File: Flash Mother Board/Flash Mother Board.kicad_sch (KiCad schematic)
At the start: 23 parts, among them IC1 RP2040_QFN56, IC2 AZ1117CH-3.3TRG1, U1 W25Q128JVS, U2 W25Q128JVS, X1 microUSB, Y1 12MHZ

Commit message: First Commit
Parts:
- removed R4: 10k, symbol Device:R
- removed U1, U2: W25Q128JVS, Package_SO:SOIC-8_5.23x5.23mm_P1.27mm, symbol Memory_Flash:W25Q128JVS
- added D1: NSR0320, Adafruit ItsyBitsy RP2040:SOD-323F, symbol Adafruit ItsyBitsy RP2040-eagle-import:DIODESOD-323F
- added J1: 104031-0811, Molex_SD:1040310811, symbol Molex_SD:104031-0811
- added R4, R5, R7: 10k, Resistor_SMD:R_0402_1005Metric, symbol Adafruit ItsyBitsy RP2040-eagle-import:RESISTOR_0402NO
- added R6: 1K, Resistor_SMD:R_0402_1005Metric, symbol Adafruit ItsyBitsy RP2040-eagle-import:RESISTOR_0402NO
- added SW1, SW2: KMR2, Adafruit ItsyBitsy RP2040:BTN_KMR2_4.6X2.8, symbol Adafruit ItsyBitsy RP2040-eagle-import:SWITCH_TACT_SMT4.6X2.8
- added TP1: TESTPOINTROUND1.5MMNO, Adafruit ItsyBitsy RP2040:TESTPOINT_ROUND_1.5MM_NO, symbol Adafruit ItsyBitsy RP2040-eagle-import:TESTPOINTROUND1.5MMNO
- added U1, U2: W25Q128JV, Package_SO:SOIC-8_5.275x5.275mm_P1.27mm, symbol Adafruit ItsyBitsy RP2040-eagle-import:SPIFLASH_8PIN_4X4
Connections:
- net +3V3: now also J1.4 (VDD), R4.1, R5.2, R7.2, U1.8 (VCC), U2.3 (WP#/IO2), U2.7 (HOLD#/IO3), U2.8 (VCC)
- net GND: now also J1.6 (VSS), SW1.B (S), SW1.B' (S1), SW2.B (S), SW2.B' (S1), U1.4 (VSS), U1.PAD (VSS), U2.4 (VSS), U2.PAD (VSS)
- net QSPI_CS: now also R4.2, R6.1, U1.1 (SSEL)
- net SPI0_MISO: now reaches IC1.27 (GPIO16)
- net SPI0_MISO: now also J1.7 (DAT0), U2.2 (MISO)
- net SPI0_CS0: now reaches IC1.28 (GPIO17)
- net SPI0_CS0: now also U2.1 (SSEL)
- net SPI0_SCK: now reaches IC1.29 (GPIO18)
- net SPI0_SCK: now also J1.5 (CLK), R5.1, U2.6 (SCK)
- net SPI0_CS1: now reaches IC1.3 (GPIO1)
- net SPI0_CS1: now also J1.2 (CD/DAT3), R7.1
- net SPI0_MOSI: now reaches IC1.30 (GPIO19)
- net SPI0_MOSI: now also J1.3 (CMD), U2.5 (MOSI)
- new net: D1.A, R6.2
- new net QSPI_DATA[0]: U1.5 (MOSI)
- new net QSPI_DATA[1]: U1.2 (MISO)
- new net QSPI_DATA[2]: U1.3 (WP#/IO2)
- new net QSPI_DATA[3]: U1.7 (HOLD#/IO3)
- new net QSPI_SCK: U1.6 (SCK)
- new net USBBOOT: D1.C, SW1.A (P), SW1.A' (P1), TP1.P$1
- new net ~{RESET}: SW2.A (P), SW2.A' (P1)
- no-connect marks 1 -> 3
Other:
- note added: "Experimental Flash"
- note added: "RESET"
- note added: "SD Card"
- moved on the sheet: C1, C10, C11, C2, C3, C4, C5, C6, C7, C8, C9, IC1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

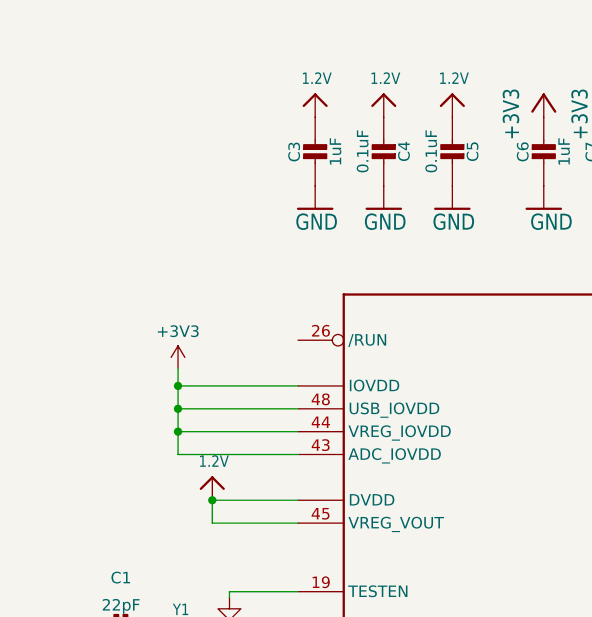
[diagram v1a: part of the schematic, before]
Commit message: Added reset line to rp2040
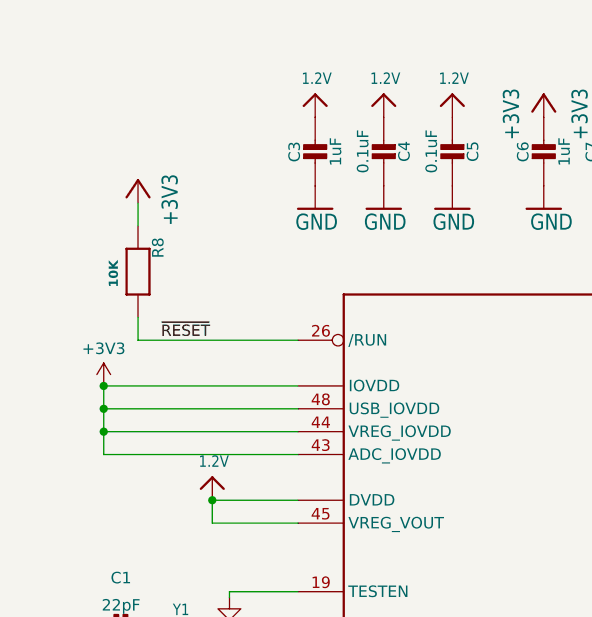
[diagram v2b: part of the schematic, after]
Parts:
- added R8: 10K, Resistor_SMD:R_0402_1005Metric, symbol Adafruit ItsyBitsy RP2040-eagle-import:RESISTOR_0402NO
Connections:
- net +3V3: now also R8.1
- net ~{RESET}: now also IC1.26 (/RUN), R8.2
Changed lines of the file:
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@@
 (kicad_sch (version 20230121) (generator eeschema)
   (paper "A4")
-  (junction (at 29.845 116.84) (diameter 0) (color 0 0 0 0)
+  (junction (at 21.59 116.84) (diameter 0) (color 0 0 0 0)
   )
   (junction (at 33.655 127) (diameter 0) (color 0 0 0 0)
@@
   (junction (at 88.138 35.56) (diameter 0) (color 0 0 0 0)
   )
-  (junction (at 29.845 114.3) (diameter 0) (color 0 0 0 0)
+  (junction (at 21.59 114.3) (diameter 0) (color 0 0 0 0)
   )
   (junction (at 262.89 86.36) (diameter 0) (color 0 0 0 0)
@@
   (junction (at 228.6 128.27) (diameter 0) (color 0 0 0 0)
   )
-  (junction (at 29.845 119.38) (diameter 0) (color 0 0 0 0)
+  (junction (at 21.59 119.38) (diameter 0) (color 0 0 0 0)
   )
   (no_connect (at 56.515 37.465))
@@
     (stroke (width 0) (type default))
   )
+  (wire (pts (xy 25.4 109.22) (xy 43.18 109.22))
+    (stroke (width 0) (type default))
+  )
   (wire (pts (xy 179.07 38.608) (xy 179.07 46.99))
     (stroke (width 0) (type default))
@@
     (stroke (width 0) (type default))
   )
-  (wire (pts (xy 29.845 116.84) (xy 29.845 119.38))
+  (wire (pts (xy 21.59 116.84) (xy 21.59 119.38))
     (stroke (width 0) (type default))
   )
@@
     (stroke (width 0) (type default))
   )
-  (wire (pts (xy 43.18 119.38) (xy 29.845 119.38))
+  (wire (pts (xy 43.18 119.38) (xy 21.59 119.38))
     (stroke (width 0) (type default))
   )
@@
     (stroke (width 0) (type default))
   )
-  (wire (pts (xy 43.18 114.3) (xy 29.845 114.3))
+  (wire (pts (xy 43.18 114.3) (xy 21.59 114.3))
     (stroke (width 0) (type default))
   )
@@
     (stroke (width 0) (type default))
   )
+  (wire (pts (xy 25.4 106.68) (xy 25.4 109.22))
+    (stroke (width 0) (type default))
+  )
   (wire (pts (xy 257.81 86.36) (xy 262.89 86.36))
     (stroke (width 0) (type default))
@@
     (stroke (width 0) (type default))
   )
-  (wire (pts (xy 43.18 121.92) (xy 29.845 121.92))
+  (wire (pts (xy 43.18 121.92) (xy 21.59 121.92))
     (stroke (width 0) (type default))
   )
@@
     (stroke (width 0) (type default))
   )
-  (wire (pts (xy 29.845 114.3) (xy 29.845 116.84))
+  (wire (pts (xy 21.59 114.3) (xy 21.59 116.84))
     (stroke (width 0) (type default))
   )
@@
     (stroke (width 0) (type default))
   )
+  (wire (pts (xy 25.4 93.98) (xy 25.4 96.52))
+    (stroke (width 0) (type default))
+  )
   (wire (pts (xy 228.6 128.27) (xy 228.6 129.54))
     (stroke (width 0) (type default))
@@
     (stroke (width 0) (type default))
   )
-  (wire (pts (xy 29.845 119.38) (xy 29.845 121.92))
+  (wire (pts (xy 21.59 119.38) (xy 21.59 121.92))
     (stroke (width 0) (type default))
   )
@@
     (stroke (width 0) (type default))
   )
-  (wire (pts (xy 29.845 112.395) (xy 29.845 114.3))
-    (stroke (width 0) (type default))
-  )
   (wire (pts (xy 255.27 21.59) (xy 255.27 19.05))
     (stroke (width 0) (type default))
   )
-  (wire (pts (xy 29.845 116.84) (xy 43.18 116.84))
+  (wire (pts (xy 21.59 116.84) (xy 43.18 116.84))
     (stroke (width 0) (type default))
   )
@@
   )
   (label "QSPI_DATA[1]" (at 189.23 44.45 0) (fields_autoplaced)
+    (effects (font (size 1.2446 1.2446)) (justify left bottom))
+  )
+  (label "~{RESET}" (at 27.94 109.22 0) (fields_autoplaced)
     (effects (font (size 1.2446 1.2446)) (justify left bottom))
   )
@@
     )
   )
-  (symbol (lib_id "power:+3V3") (at 29.845 112.395 0) (unit 1)
+  (symbol (lib_id "power:+3V3") (at 21.59 114.3 0) (unit 1)
     (in_bom yes) (on_board yes) (dnp no) (fields_autoplaced)
-    (property "Reference" "#PWR03" (at 29.845 116.205 0)
-      (effects (font (size 1.27 1.27)) hide)
-    )
-    (property "Value" "+3V3" (at 29.845 108.2619 0)
-      (effects (font (size 1.27 1.27)))
-    )
-    (property "Footprint" "" (at 29.845 112.395 0)
-      (effects (font (size 1.27 1.27)) hide)
-    )
-    (property "Datasheet" "" (at 29.845 112.395 0)
+    (property "Reference" "#PWR03" (at 21.59 118.11 0)
+      (effects (font (size 1.27 1.27)) hide)
+    )
+    (property "Value" "+3V3" (at 21.59 110.1669 0)
+      (effects (font (size 1.27 1.27)))
+    )
+    (property "Footprint" "" (at 21.59 114.3 0)
+      (effects (font (size 1.27 1.27)) hide)
+    )
+    (property "Datasheet" "" (at 21.59 114.3 0)
       (effects (font (size 1.27 1.27)) hide)
     )
@@
     )
   )
+  (symbol (lib_id "Adafruit ItsyBitsy RP2040-eagle-import:+3V3") (at 25.4 91.44 0) (mirror y) (unit 1)
+    (in_bom yes) (on_board yes) (dnp no)
+    (property "Reference" "#+3V011" (at 25.4 91.44 0)
+      (effects (font (size 1.27 1.27)) hide)
+    )
+    (property "Value" "+3V3" (at 27.94 96.52 90)
+      (effects (font (size 1.778 1.5113)) (justify left bottom))
+    )
+    (property "Footprint" "Adafruit ItsyBitsy RP2040:" (at 25.4 91.44 0)
+      (effects (font (size 1.27 1.27)) hide)
+    )
+    (property "Datasheet" "" (at 25.4 91.44 0)
+      (effects (font (size 1.27 1.27)) hide)
+    )
+    (pin "1")
+    (instances
+      (project "Flash Mother Board"
+        (path "/f8edefc2-0888-457d-9803-46e1c7e584b2"
+          (reference "#+3V011") (unit 1)
+        )
+      )
+    )
+  )
   (symbol (lib_id "Device:R") (at 60.325 34.925 90) (unit 1)
     (in_bom yes) (on_board yes) (dnp no)
@@
         )
       )
+    )
+  )
+  (symbol (lib_id "Adafruit ItsyBitsy RP2040-eagle-import:RESISTOR_0402NO") (at 25.4 101.6 270) (unit 1)
+    (in_bom yes) (on_board yes) (dnp no)
+    (property "Reference" "R8" (at 26.8986 97.79 0)
+      (effects (font (size 1.27 1.27)) (justify left bottom))
+    )
+    (property "Value" "10K" (at 22.098 100.33 0)
+      (effects (font (size 1.016 1.016) bold) (justify left bottom))
+    )
+    (property "Footprint" "Resistor_SMD:R_0402_1005Metric" (at 25.4 101.6 0)
+      (effects (font (size 1.27 1.27)) hide)
+    )
+    (property "Datasheet" "" (at 25.4 101.6 0)
+      (effects (font (size 1.27 1.27)) hide)
+    )
+    (pin "1")
+    (pin "2")
+    (instances
+      (project "Flash Mother Board"
+        (path "/f8edefc2-0888-457d-9803-46e1c7e584b2"
+          (reference "R8") (unit 1)
+        )
+      )

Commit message: All Footprints Added
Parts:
- IC1: footprint RO2040_Feather:QFN56_7MM_REDUCEDEPAD -> Adafruit ItsyBitsy RP2040:QFN56_7MM_REDUCEDEPAD
- R1, R2, R3: footprint (none) -> Resistor_SMD:R_0402_1005Metric
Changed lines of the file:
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@@
       (effects (font (size 1.27 1.27)))
     )
-    (property "Footprint" "" (at 37.465 146.558 90)
+    (property "Footprint" "Resistor_SMD:R_0402_1005Metric" (at 37.465 146.558 90)
       (effects (font (size 1.27 1.27)) hide)
     )
@@
       (effects (font (size 1.778 1.5113)) (justify left bottom))
     )
-    (property "Footprint" "RO2040_Feather:QFN56_7MM_REDUCEDEPAD" (at 81.28 147.32 0)
+    (property "Footprint" "Adafruit ItsyBitsy RP2040:QFN56_7MM_REDUCEDEPAD" (at 81.28 147.32 0)
       (effects (font (size 1.27 1.27)) hide)
     )
@@
       (effects (font (size 1.27 1.27)))
     )
-    (property "Footprint" "" (at 60.325 34.163 90)
+    (property "Footprint" "Resistor_SMD:R_0402_1005Metric" (at 60.325 34.163 90)
       (effects (font (size 1.27 1.27)) hide)
     )
@@
     )
   )
-  (symbol (lib_id "AZ1117CH-3.3TRG1:AZ1117CH-3.3TRG1") (at 91.44 30.48 0) (unit 1)
-    (in_bom yes) (on_board yes) (dnp no) (fields_autoplaced)
-    (property "Reference" "IC2" (at 107.95 22.86 0)
-      (effects (font (size 1.27 1.27)))
-    )
-    (property "Value" "AZ1117CH-3.3TRG1" (at 107.95 25.4 0)
-      (effects (font (size 1.27 1.27)))
-    )
-    (property "Footprint" "3.3VRegForUSB:SOT230P700X180-4N" (at 120.65 27.94 0)
-      (effects (font (size 1.27 1.27)) (justify left) hide)
-    )
-    (property "Datasheet" "https://datasheet.datasheetarchive.com/originals/distributors/Datasheets-DGA25/1776204.pdf" (at 120.65 30.48 0)
-      (effects (font (size 1.27 1.27)) (justify left) hide)
-    )
-    (property "Description" "1.35A 3.3V LDO Reg. Current Limit SOT223 DiodesZetex AZ1117CH-3.3TRG1, LDO Voltage Regulator, 0.8A, 3.3 V +/-1%, maximum of 15 Vin, 3-Pin SOT-223" (at 120.65 33.02 0)
-      (effects (font (size 1.27 1.27)) (justify left) hide)
-    )
-    (property "Height" "1.8" (at 120.65 35.56 0)
-      (effects (font (size 1.27 1.27)) (justify left) hide)
-    )
-    (property "Mouser Part Number" "621-AZ1117CH-3.3TRG1" (at 120.65 38.1 0)
-      (effects (font (size 1.27 1.27)) (justify left) hide)
-    )
-    (property "Mouser Price/Stock" "https://www.mouser.co.uk/ProductDetail/Diodes-Incorporated/AZ1117CH-3.3TRG1?qs=FKu9oBikfSm7ntaG6olPSQ%3D%3D" (at 120.65 40.64 0)
-      (effects (font (size 1.27 1.27)) (justify left) hide)
-    )
-    (property "Manufacturer_Name" "Diodes Inc." (at 120.65 43.18 0)
-      (effects (font (size 1.27 1.27)) (justify left) hide)
-    )
-    (property "Manufacturer_Part_Number" "AZ1117CH-3.3TRG1" (at 120.65 45.72 0)
-      (effects (font (size 1.27 1.27)) (justify left) hide)
-    )
-    (pin "1")
-    (pin "2")
-    (pin "3")
-    (pin "4")
-    (instances
-      (project "FC_Board_v3"
-        (path "/e63e39d7-6ac0-4ffd-8aa3-1841a4541b55"
-          (reference "IC2") (unit 1)
-        )
-      )
-      (project "Flash Mother Board"
-        (path "/f8edefc2-0888-457d-9803-46e1c7e584b2"
-          (reference "IC2") (unit 1)
-        )
-      )
-    )
-  )
   (symbol (lib_id "power:+3V3") (at 129.54 30.48 0) (unit 1)
     (in_bom yes) (on_board yes) (dnp no) (fields_autoplaced)
@@
       (effects (font (size 1.27 1.27)))
     )
-    (property "Footprint" "" (at 60.325 36.703 90)
+    (property "Footprint" "Resistor_SMD:R_0402_1005Metric" (at 60.325 36.703 90)
       (effects (font (size 1.27 1.27)) hide)
     )
@@
         )
       )
+    )
+  )
+  (symbol (lib_name "AZ1117CH-3.3TRG1_1") (lib_id "AZ1117CH-3.3TRG1:AZ1117CH-3.3TRG1") (at 91.44 30.48 0) (unit 1)
+    (in_bom yes) (on_board yes) (dnp no) (fields_autoplaced)
+    (property "Reference" "IC2" (at 107.95 22.86 0)
+      (effects (font (size 1.27 1.27)))
+    )
+    (property "Value" "AZ1117CH-3.3TRG1" (at 107.95 25.4 0)
+      (effects (font (size 1.27 1.27)))
+    )
+    (property "Footprint" "3.3VRegForUSB:SOT230P700X180-4N" (at 120.65 27.94 0)
+      (effects (font (size 1.27 1.27)) (justify left) hide)
+    )
+    (property "Datasheet" "https://datasheet.datasheetarchive.com/originals/distributors/Datasheets-DGA25/1776204.pdf" (at 120.65 30.48 0)
+      (effects (font (size 1.27 1.27)) (justify left) hide)
+    )
+    (property "Description" "1.35A 3.3V LDO Reg. Current Limit SOT223 DiodesZetex AZ1117CH-3.3TRG1, LDO Voltage Regulator, 0.8A, 3.3 V +/-1%, maximum of 15 Vin, 3-Pin SOT-223" (at 120.65 33.02 0)
+      (effects (font (size 1.27 1.27)) (justify left) hide)
+    )
+    (property "Height" "1.8" (at 120.65 35.56 0)
+      (effects (font (size 1.27 1.27)) (justify left) hide)
+    )
+    (property "Mouser Part Number" "621-AZ1117CH-3.3TRG1" (at 120.65 38.1 0)
+      (effects (font (size 1.27 1.27)) (justify left) hide)
+    )
+    (property "Mouser Price/Stock" "https://www.mouser.co.uk/ProductDetail/Diodes-Incorporated/AZ1117CH-3.3TRG1?qs=FKu9oBikfSm7ntaG6olPSQ%3D%3D" (at 120.65 40.64 0)
+      (effects (font (size 1.27 1.27)) (justify left) hide)
+    )
+    (property "Manufacturer_Name" "Diodes Inc." (at 120.65 43.18 0)
+      (effects (font (size 1.27 1.27)) (justify left) hide)
+    )
+    (property "Manufacturer_Part_Number" "AZ1117CH-3.3TRG1" (at 120.65 45.72 0)
+      (effects (font (size 1.27 1.27)) (justify left) hide)
+    )
+    (pin "2")
+    (pin "3")
+    (pin "4")
+    (pin "1")
+    (instances
+      (project "Flash Mother Board"
+        (path "/f8edefc2-0888-457d-9803-46e1c7e584b2"
+          (reference "IC2") (unit 1)
+        )
+      )

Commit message: More Routing Autosave
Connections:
- net QSPI_DATA[0] is gone; now on net QSPI_SD0: U1.5 (MOSI)
- net QSPI_DATA[1] is gone; now on net QSPI_SD1: U1.2 (MISO)
- net QSPI_DATA[2] is gone; now on net QSPI_SD2: U1.3 (WP#/IO2)
- net QSPI_DATA[3] is gone; now on net QSPI_SD3: U1.7 (HOLD#/IO3)
- net QSPI_SCK is gone; now on net QSPI_SCLK: U1.6 (SCK)
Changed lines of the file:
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@@
+    (stroke (width 0) (type default))
+  )
+  (wire (pts (xy 88.9 33.02) (xy 91.44 33.02))
     (stroke (width 0) (type default))
   )
@@
     (stroke (width 0) (type default))
   )
+  (wire (pts (xy 88.9 27.94) (xy 88.9 33.02))
+    (stroke (width 0) (type default))
+  )
   (wire (pts (xy 257.81 54.61) (xy 257.81 59.69))
     (stroke (width 0) (type default))
@@
   )
   (wire (pts (xy 257.81 104.14) (xy 257.81 86.36))
-    (stroke (width 0) (type default))
-  )
-  (wire (pts (xy 87.884 33.02) (xy 91.44 33.02))
     (stroke (width 0) (type default))
   )
@@
     (effects (font (size 1.2446 1.2446)) (justify left bottom))
   )
-  (label "QSPI_SCK" (at 189.23 39.37 0) (fields_autoplaced)
+  (label "QSPI_SCLK" (at 189.23 39.37 0) (fields_autoplaced)
     (effects (font (size 1.2446 1.2446)) (justify left bottom))
   )
@@
     (effects (font (size 1.27 1.27)) (justify right bottom))
   )
-  (label "QSPI_DATA[2]" (at 189.23 49.53 0) (fields_autoplaced)
+  (label "QSPI_SD2" (at 189.23 49.53 0) (fields_autoplaced)
     (effects (font (size 1.2446 1.2446)) (justify left bottom))
   )
-  (label "QSPI_DATA[3]" (at 189.23 52.07 0) (fields_autoplaced)
+  (label "QSPI_SD3" (at 189.23 52.07 0) (fields_autoplaced)
     (effects (font (size 1.2446 1.2446)) (justify left bottom))
   )
@@
     (effects (font (size 1.27 1.27)) (justify right bottom))
   )
-  (label "QSPI_DATA[0]" (at 189.23 41.91 0) (fields_autoplaced)
+  (label "QSPI_SD0" (at 189.23 41.91 0) (fields_autoplaced)
     (effects (font (size 1.2446 1.2446)) (justify left bottom))
   )
@@
     (effects (font (size 1.27 1.27)) (justify left bottom))
   )
-  (label "QSPI_DATA[1]" (at 189.23 44.45 0) (fields_autoplaced)
+  (label "QSPI_SD1" (at 189.23 44.45 0) (fields_autoplaced)
     (effects (font (size 1.2446 1.2446)) (justify left bottom))
   )
@@
     )
   )
-  (symbol (lib_id "power:+3V3") (at 87.884 33.02 0) (unit 1)
+  (symbol (lib_id "power:+3V3") (at 88.9 27.94 0) (unit 1)
     (in_bom yes) (on_board yes) (dnp no) (fields_autoplaced)
-    (property "Reference" "#PWR0105" (at 87.884 36.83 0)
-      (effects (font (size 1.27 1.27)) hide)
-    )
-    (property "Value" "+3V3" (at 87.884 29.4442 0)
-      (effects (font (size 1.27 1.27)))
-    )
-    (property "Footprint" "" (at 87.884 33.02 0)
-      (effects (font (size 1.27 1.27)) hide)
-    )
-    (property "Datasheet" "" (at 87.884 33.02 0)
-      (effects (font (size 1.27 1.27)) hide)
-    )
+    (property "Reference" "#PWR0105" (at 88.9 31.75 0)
+      (effects (font (size 1.27 1.27)) hide)
+    )
+    (property "Value" "+3V3" (at 88.9 24.3642 0)
+      (effects (font (size 1.27 1.27)))
+    )
+    (property "Footprint" "" (at 88.9 27.94 0)
+      (effects (font (size 1.27 1.27)) hide)
+    )
+    (property "Datasheet" "" (at 88.9 27.94 0)
+      (effects (font (size 1.27 1.27)) hide)
+    )

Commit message: Routing Almost Complete
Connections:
- net GND: now also X1.5 (GND); no longer X1.BASE@1 (GND)
- net SPI0_CS0: now also R5.1
- net SPI0_SCK: no longer R5.1
- net VBUS: now also X1.1 (VBUS); no longer X1.VBUS
- net at R1.1: now also X1.2 (D+); no longer X1.D+
- net at R2.1: now also X1.3 (D-); no longer X1.D-
